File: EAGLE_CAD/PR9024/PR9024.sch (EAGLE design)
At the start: 70 parts, among them SW1 C&K_PTS645, U1 SI4702-C19-GMR, X1 ABS25XTAL

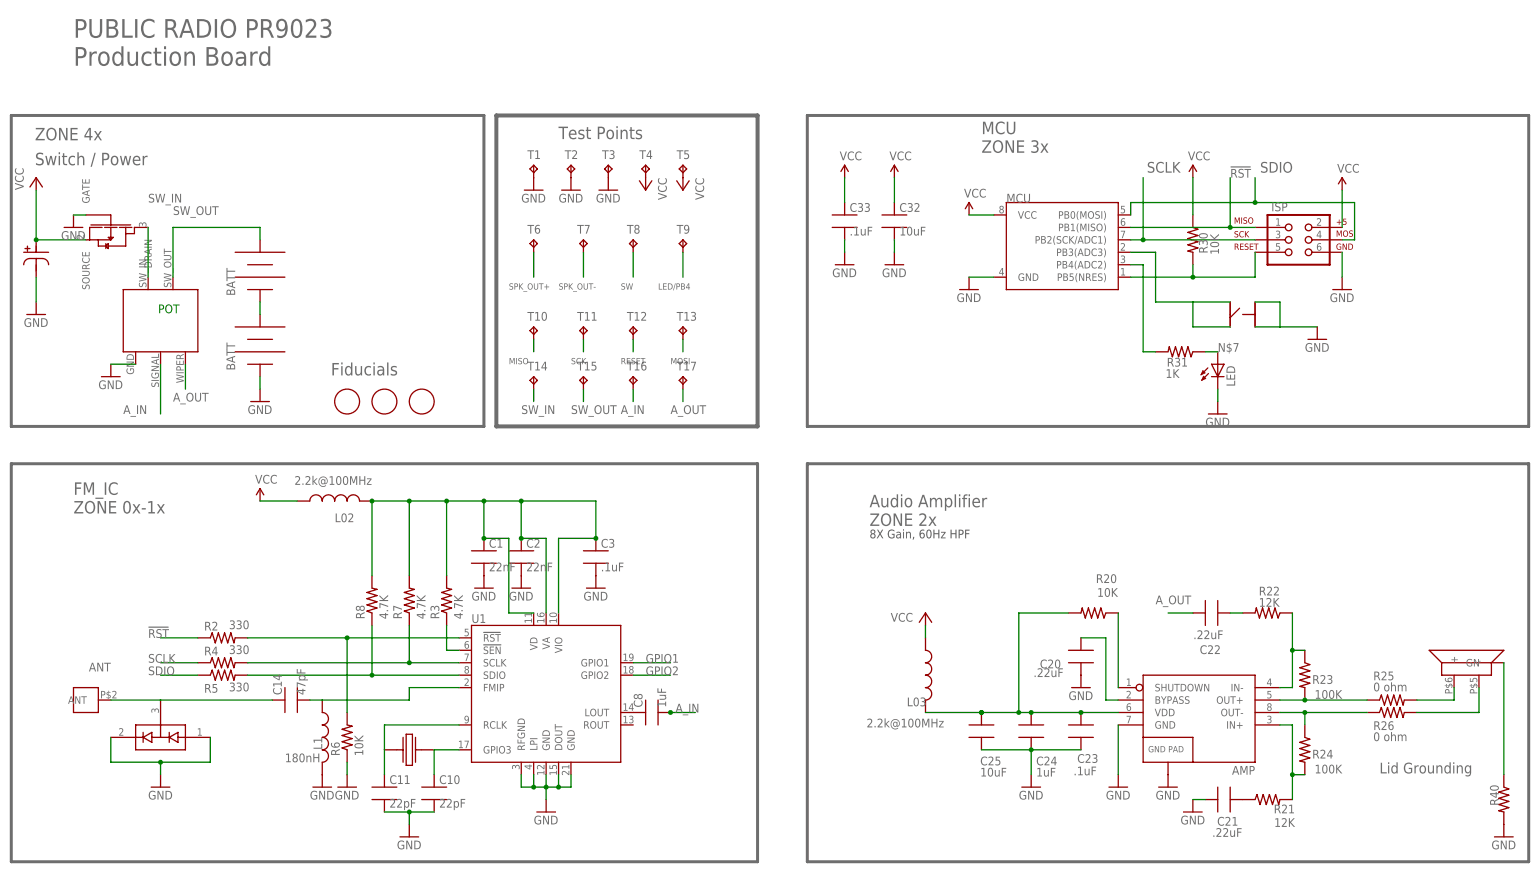
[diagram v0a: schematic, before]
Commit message: Updated Speaker Placement
Disconnected the SMT PEM nut placements from the speaker so the gerbers
reflect these as separate parts and placements.
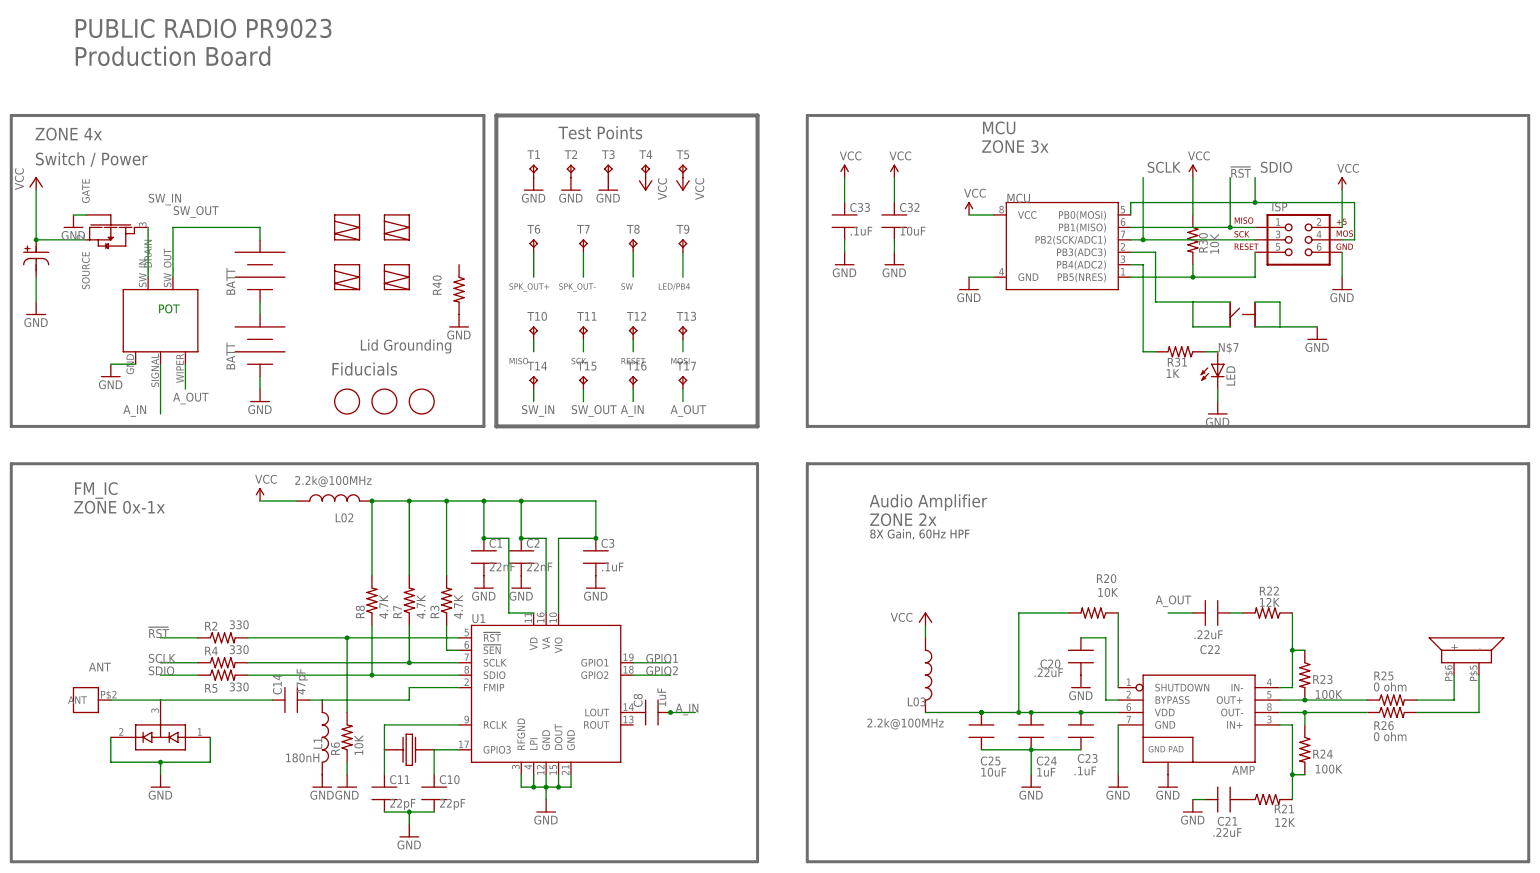
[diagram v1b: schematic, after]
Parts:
- added U$2, U$3, U$4, U$5: PEM_SMT, PR_Parts_Library:PEM_SMT
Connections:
- removed net N$6: R40.1, SPKR_PLACE.GN
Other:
- moved on the sheet: R40
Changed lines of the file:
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@@
 <attribute name="MFG_PN" value="ERJ-6GEY0R00V "/>
 </part>
+<part name="U$2" library="PR_Parts_Library" deviceset="PEM_SMT" device=""/>
+<part name="U$3" library="PR_Parts_Library" deviceset="PEM_SMT" device=""/>
+<part name="U$4" library="PR_Parts_Library" deviceset="PEM_SMT" device=""/>
+<part name="U$5" library="PR_Parts_Library" deviceset="PEM_SMT" device=""/>
 </parts>
 <sheets>
@@
 ZONE 0x-1x</text>
 <text x="-35.814" y="142.24" size="2.54" layer="96">Switch / Power  </text>
-<text x="238.76" y="18.034" size="2.1844" layer="96">Lid Grounding</text>
+<text x="30.48" y="104.394" size="2.1844" layer="96">Lid Grounding</text>
 <text x="134.62" y="68.58" size="2.54" layer="96">Audio Amplifier
 ZONE 2x</text>
@@
 <instance part="GND5" gate="1" x="-20.32" y="99.06"/>
 <instance part="GND2" gate="1" x="-35.56" y="111.76"/>
-<instance part="GND12" gate="1" x="264.16" y="5.08"/>
+<instance part="GND12" gate="1" x="50.8" y="109.22"/>
 <instance part="GND3" gate="1" x="-27.94" y="129.54"/>
 <instance part="MCU" gate="G$1" x="175.26" y="124.46"/>
@@
 <attribute name="VALUE" x="176.276" y="17.653" size="1.778" layer="96"/>
 </instance>
-<instance part="R40" gate="G$1" x="264.16" y="12.7" smashed="yes" rot="R270">
-<attribute name="NAME" x="263.1186" y="11.43" size="1.778" layer="95" rot="R90"/>
+<instance part="R40" gate="G$1" x="50.8" y="116.84" smashed="yes" rot="R270">
+<attribute name="NAME" x="47.2186" y="115.57" size="1.778" layer="95" rot="R90"/>
 </instance>
 <instance part="D1" gate="G$1" x="-10.16" y="25.4" rot="R180"/>
@@
 <attribute name="VALUE" x="237.49" y="24.638" size="1.778" layer="96"/>
 </instance>
+<instance part="U$2" gate="G$1" x="27.94" y="129.54"/>
+<instance part="U$3" gate="G$1" x="38.1" y="129.54"/>
+<instance part="U$4" gate="G$1" x="27.94" y="119.38"/>
+<instance part="U$5" gate="G$1" x="38.1" y="119.38"/>
 </instances>
 <busses>
@@
 <pinref part="R25" gate="G$1" pin="2"/>
 <pinref part="SPKR_PLACE" gate="G$1" pin="+"/>
-<wire x1="254" y1="33.02" x2="254" y2="35.56" width="0.1524" layer="91"/>
+<wire x1="254" y1="33.02" x2="254" y2="38.1" width="0.1524" layer="91"/>
 </segment>
 </net>
@@
 <wire x1="246.38" y1="30.48" x2="259.08" y2="30.48" width="0.1524" layer="91"/>
 <pinref part="SPKR_PLACE" gate="G$1" pin="-"/>
-<wire x1="259.08" y1="30.48" x2="259.08" y2="35.56" width="0.1524" layer="91"/>
+<wire x1="259.08" y1="30.48" x2="259.08" y2="38.1" width="0.1524" layer="91"/>
 </segment>
 </net>
@@
 </segment>
 </net>
-<net name="N$6" class="0">
-<segment>
-<pinref part="SPKR_PLACE" gate="G$1" pin="GN"/>
-<pinref part="R40" gate="G$1" pin="1"/>
-<wire x1="264.16" y1="40.64" x2="264.16" y2="17.78" width="0.1524" layer="91"/>
-</segment>
-</net>

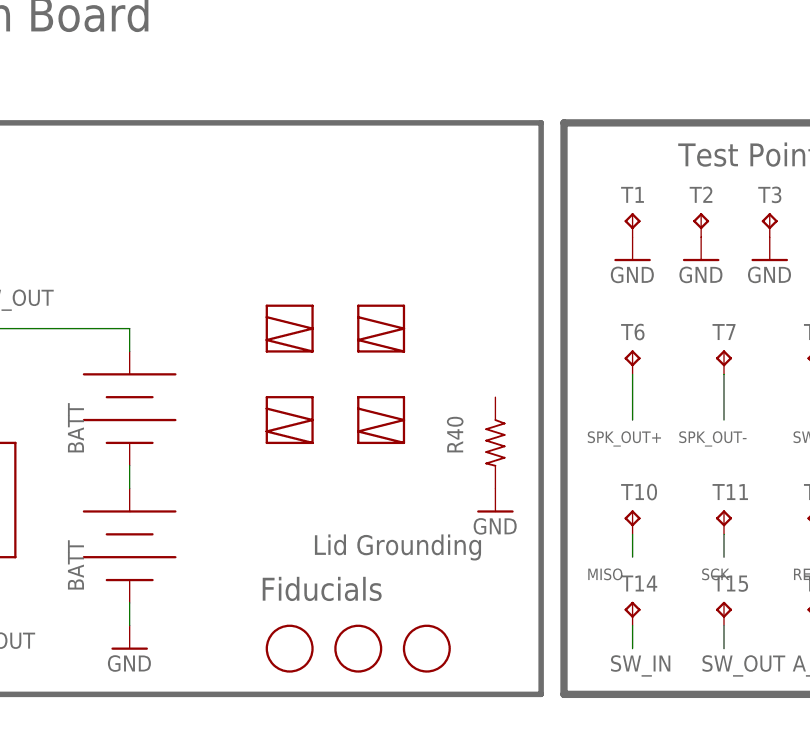
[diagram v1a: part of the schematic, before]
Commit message: PR9024 & PR9001 Updates
-Small changes to PR9024
-New, simple programming board, PR9001 to connect to ISP pads and two
ground pads only.
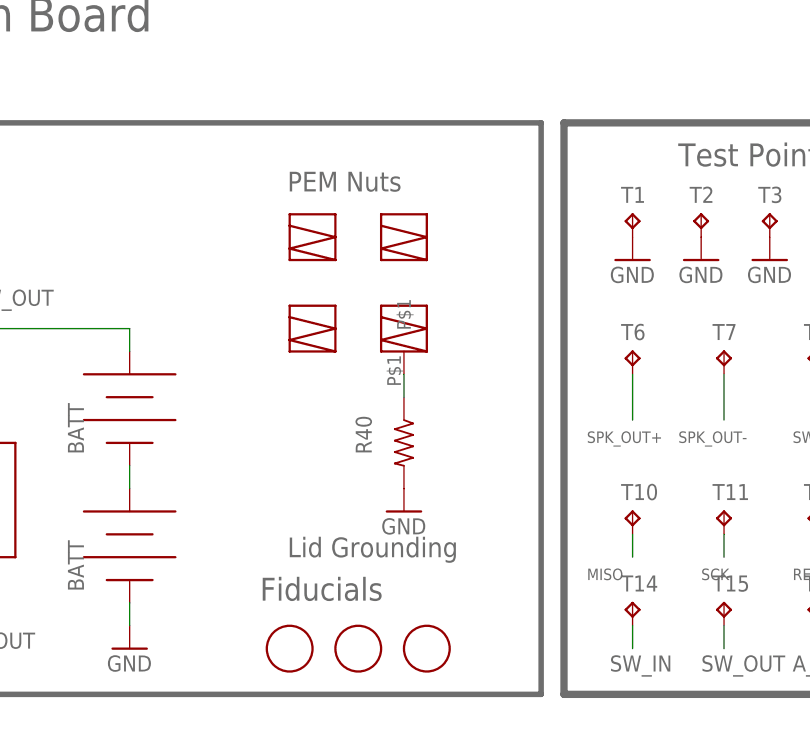
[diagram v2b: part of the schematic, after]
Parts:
- U$5: value PEM_SMT -> PEM_M3_SMT_W/PIN; device PR_Parts_Library:PEM_SMT -> PR_Parts_Library:PEM_M3_SMT_W/PIN
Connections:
- new net N$6: R40.1, U$5.P$1
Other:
- note added: "PEM Nuts"
- moved on the sheet: R40
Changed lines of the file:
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@@
 <part name="U$3" library="PR_Parts_Library" deviceset="PEM_SMT" device=""/>
 <part name="U$4" library="PR_Parts_Library" deviceset="PEM_SMT" device=""/>
-<part name="U$5" library="PR_Parts_Library" deviceset="PEM_SMT" device=""/>
+<part name="U$5" library="PR_Parts_Library" deviceset="PEM_M3_SMT_W/PIN" device=""/>
 </parts>
 <sheets>
@@
 ZONE 0x-1x</text>
 <text x="-35.814" y="142.24" size="2.54" layer="96">Switch / Power  </text>
-<text x="30.48" y="104.394" size="2.1844" layer="96">Lid Grounding</text>
+<text x="27.686" y="104.14" size="2.1844" layer="96">Lid Grounding</text>
 <text x="134.62" y="68.58" size="2.54" layer="96">Audio Amplifier
 ZONE 2x</text>
@@
 <text x="134.62" y="66.04" size="1.778" layer="97">8X Gain, 60Hz HPF</text>
 <text x="-35.814" y="147.32" size="2.54" layer="96">ZONE 4x</text>
+<text x="27.686" y="144.78" size="2.1844" layer="96">PEM Nuts</text>
 </plain>
 <instances>
@@
 <instance part="GND5" gate="1" x="-20.32" y="99.06"/>
 <instance part="GND2" gate="1" x="-35.56" y="111.76"/>
-<instance part="GND12" gate="1" x="50.8" y="109.22"/>
+<instance part="GND12" gate="1" x="40.64" y="109.22"/>
 <instance part="GND3" gate="1" x="-27.94" y="129.54"/>
 <instance part="MCU" gate="G$1" x="175.26" y="124.46"/>
@@
 <attribute name="VALUE" x="176.276" y="17.653" size="1.778" layer="96"/>
 </instance>
-<instance part="R40" gate="G$1" x="50.8" y="116.84" smashed="yes" rot="R270">
-<attribute name="NAME" x="47.2186" y="115.57" size="1.778" layer="95" rot="R90"/>
+<instance part="R40" gate="G$1" x="40.64" y="116.84" smashed="yes" rot="R270">
+<attribute name="NAME" x="37.0586" y="115.57" size="1.778" layer="95" rot="R90"/>
 </instance>
 <instance part="D1" gate="G$1" x="-10.16" y="25.4" rot="R180"/>
@@
 <attribute name="VALUE" x="237.49" y="24.638" size="1.778" layer="96"/>
 </instance>
-<instance part="U$2" gate="G$1" x="27.94" y="129.54"/>
-<instance part="U$3" gate="G$1" x="38.1" y="129.54"/>
-<instance part="U$4" gate="G$1" x="27.94" y="119.38"/>
-<instance part="U$5" gate="G$1" x="38.1" y="119.38"/>
+<instance part="U$2" gate="G$1" x="30.48" y="139.7"/>
+<instance part="U$3" gate="G$1" x="40.64" y="139.7"/>
+<instance part="U$4" gate="G$1" x="30.48" y="129.54"/>
+<instance part="U$5" gate="G$1" x="40.64" y="129.54"/>
 </instances>
 <busses>
@@
 </segment>
 </net>
+<net name="N$6" class="0">
+<segment>
+<pinref part="U$5" gate="G$1" pin="P$1"/>
+<pinref part="R40" gate="G$1" pin="1"/>
+<wire x1="40.64" y1="121.92" x2="40.64" y2="124.46" width="0.1524" layer="91"/>
+</segment>
+</net>

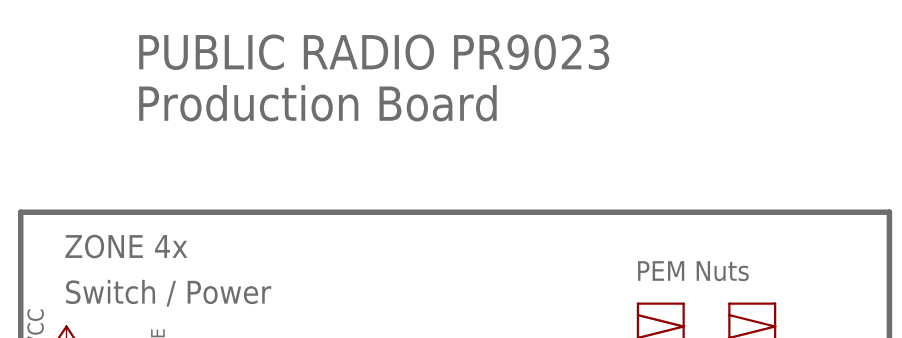
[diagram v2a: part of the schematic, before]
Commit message: updated pot & rerouted stuff
new pot is Hong Yu Innovation Electronics Co
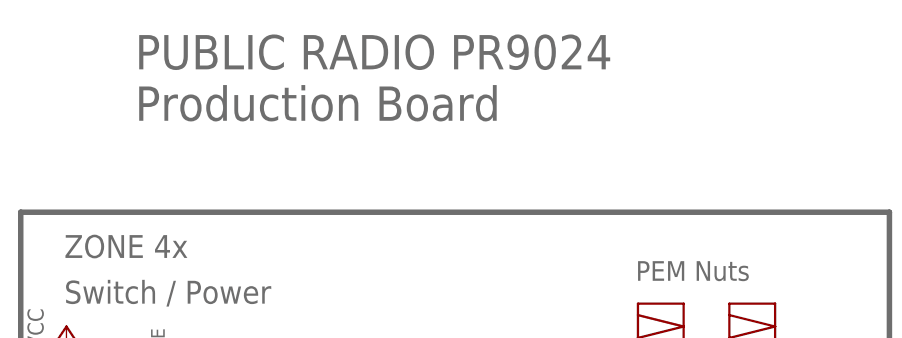
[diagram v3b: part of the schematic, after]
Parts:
- R1: value RV170SF_TAIWANA_POT_SW -> VOLUME_POT; device PR_Parts_Library:RV170SF_TAIWANA_POT_SW -> PR_Parts_Library:VOLUME_POT; MFG_PN RV170SF-43-20F-A10K - supplied by CL Labs -> (none)
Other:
- note added: "PUBLIC RADIO PR9024 Production Board"
- note removed: "PUBLIC RADIO PR9023 Production Board"
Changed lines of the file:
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@@
 <?xml version="1.0" encoding="utf-8"?>
 <!DOCTYPE eagle SYSTEM "eagle.dtd">
-<eagle version="6.6.0">
+<eagle version="7.7.0">
 <drawing>
 <settings>
@@
 <part name="P+1" library="supply1" deviceset="VCC" device=""/>
 <part name="ANT_MOUNT" library="PR_Parts_Library" deviceset="M3_PEMNUT" device="" value="DNP"/>
-<part name="R1" library="PR_Parts_Library" deviceset="RV170SF_TAIWANA_POT_SW" device="" value="">
-<attribute name="MFG_PN" value="RV170SF-43-20F-A10K - supplied by CL Labs"/>
-</part>
+<part name="R1" library="PR_Parts_Library" deviceset="VOLUME_POT" device="" value="VOLUME_POT"/>
 <part name="GND5" library="SparkFun-Aesthetics" deviceset="GND" device=""/>
 <part name="GND2" library="SparkFun-Aesthetics" deviceset="GND" device=""/>
@@
 <text x="157.48" y="144.78" size="2.54" layer="96">MCU
 ZONE 3x</text>
-<text x="-27.94" y="162.56" size="3.81" layer="96">PUBLIC RADIO PR9023
+<text x="-27.94" y="162.56" size="3.81" layer="96">PUBLIC RADIO PR9024
 Production Board </text>
 <text x="24.638" y="99.314" size="2.54" layer="96">Fiducials </text>

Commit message: Reverse Mount LED
added a reverse mount LED to our library and populated the board with
it.
https://www.digikey.com/product-detail/en/broadcom-limited/HSMC-C265/516
-1465-2-ND/637725
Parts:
- LED: value (none) -> HSMC-C265_REVERSE_MOUNT_LED; device adafruit:LEDCHIPLED_0805 -> PR_Parts_Library:HSMC-C265_REVERSE_MOUNT_LED; MFG_PN LY R976-PS-36 -> HSMC-C265
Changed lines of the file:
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@@
 <attribute name="TOL" value="1%"/>
 </part>
-<part name="LED" library="adafruit" deviceset="LED" device="CHIPLED_0805">
-<attribute name="MFG_PN" value="LY R976-PS-36"/>
+<part name="LED" library="PR_Parts_Library" deviceset="HSMC-C265_REVERSE_MOUNT_LED" device="">
+<attribute name="MFG_PN" value="HSMC-C265"/>
 </part>
 <part name="R25" library="PR_Parts_Library" deviceset="R_SMT" device="_0805_ADAFRUIT" value="0 ohm">
